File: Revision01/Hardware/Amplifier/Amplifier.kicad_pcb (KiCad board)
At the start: 2 copper layers, 23 x 13.5 mm, 13 parts, among them U1 INA333AIDGKR, U2 TLV9061SQDBVRQ1

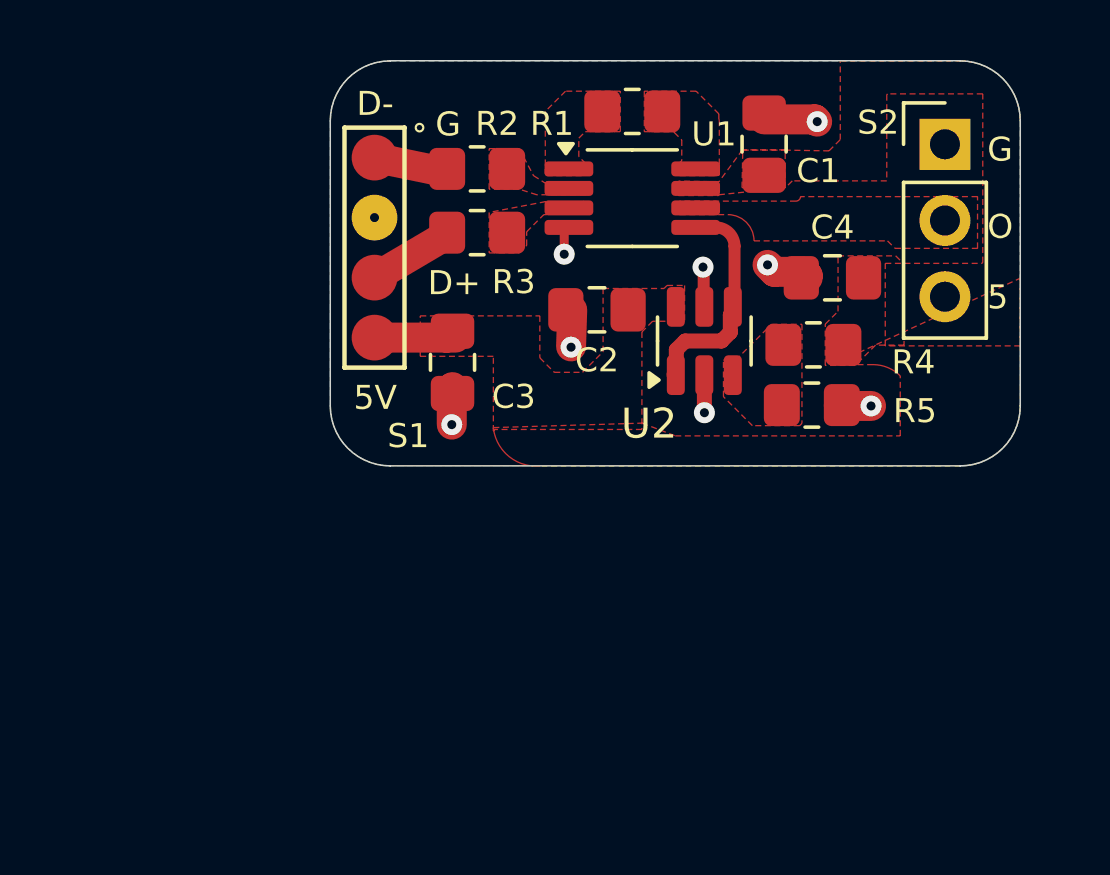
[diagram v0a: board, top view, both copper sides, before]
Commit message: . Amplifier layout WIP draft with 500 ohm resistor . Hub layout final draft, added 100 ohm series resistor to AIN
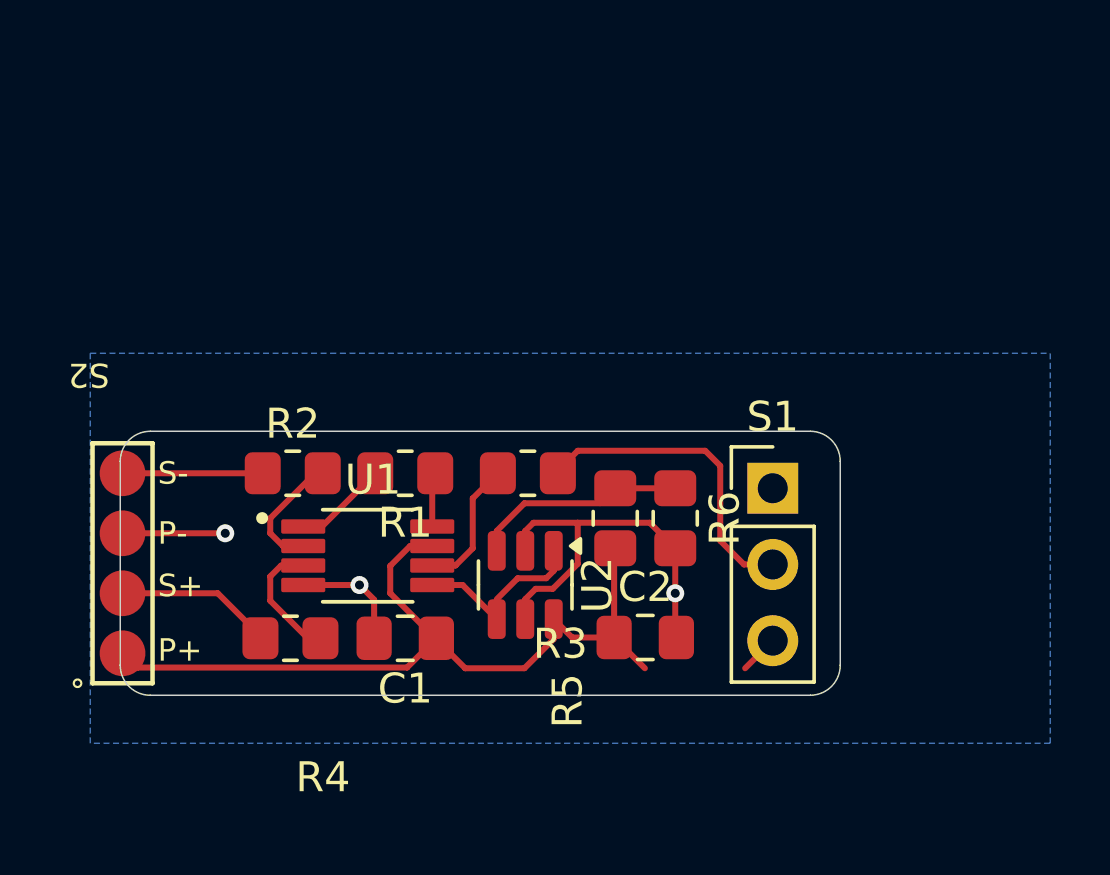
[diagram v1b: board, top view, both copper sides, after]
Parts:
- removed C3, C4: 0.1uF, Capacitor_SMD:C_0805_2012Metric_Pad1.18x1.45mm_HandSolder
- added R6: 100K +-0.1%, Resistor_SMD:R_0805_2012Metric_Pad1.20x1.40mm_HandSolder, F.Cu at (148.5, 113.5)
- R3: value 1K +-0.1% -> 500 ± 5%
- R4: value 200K +-0.1% -> 1K +-0.1%
- R5: value 100K +-0.1% -> 200K +-0.1%
- S1: value CONN_01X04_StrainGauge -> CONN_01X03_2.54MM; footprint StrainAmplifierV1:CONN_01X04 -> Connector_PinHeader_2.54mm:PinHeader_1x03_P2.54mm_Vertical
- S2: value CONN_01X03_2.54MM -> CONN_01X04_StrainGauge; footprint Connector_PinHeader_2.54mm:PinHeader_1x03_P2.54mm_Vertical -> Amplifier:CONN_01X04
- U1: footprint Package_SO:VSSOP-8_3x3mm_P0.65mm -> Amplifier:INA333AIDGKR_SOP65P490X110-8N
- moved S2 32.2 mm to (130.1, 118.0), turned to 180 degrees
- moved C1 20.4 mm to (139.5, 117.5), turned to 180 degrees
- moved R4 20.0 mm to (135.7, 117.5), turned to 180 degrees
- moved S1 17.3 mm to (151.8, 112.5)
- moved U1 14.8 mm to (138.2, 114.8)
- moved R1 14.2 mm to (139.5, 112.0)
- moved R2 11.9 mm to (135.8, 112.0), turned to 0 degrees
- moved C2 11.0 mm to (147.5, 117.5), turned to 0 degrees
- moved U2 10.1 mm to (143.5, 115.7), turned to -90 degrees
- moved R3 8.20 mm to (143.6, 112.0)
- moved R5 7.56 mm to (146.5, 113.5), turned to 90 degrees
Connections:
- R2 pad 1: Net-(U1-VIN-) -> /strainAIN_D-
- R2 pad 2: /strainAIN_D- -> Net-(U1-VIN-)
- R3 pad 1: Net-(U1-VIN+) -> Net-(S1-Pin_2)
- R3 pad 2: /strainAIN_D+ -> Net-(U1-VOUT)
- R4 pad 1: Net-(U2-IN+) -> Net-(U1-VIN+)
- R4 pad 2: +5V -> /strainAIN_D+
- R5 pad 1: GND -> +5V
- S1 pad 1: /strainAIN_D- -> GND
- S1 pad 2: GND -> Net-(S1-Pin_2)
- S1 pad 3: /strainAIN_D+ -> +5V
- S2 pad 1: GND -> +5V
- S2 pad 2: Net-(U1-VOUT) -> /strainAIN_D+
- S2 pad 3: +5V -> GND
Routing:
- net +5V: track 2.95 -> 29.7 mm
- net Net-(S1-Pin_2): track 0.00 -> 11.1 mm
- net GND: track 10.2 -> 20.3 mm, vias 8 -> 3
- net Net-(U2-IN+): track 0.00 -> 7.42 mm
- net Net-(U1-VOUT): track 0.00 -> 4.50 mm
- net Net-(U1-VIN+): track 0.00 -> 4.25 mm
- net Net-(U1-VIN-): track 0.00 -> 4.15 mm
- net Net-(R1-Pad2): track 0.00 -> 3.14 mm
- net /strainAIN_D+: track 2.90 -> 4.94 mm
- net /strainAIN_D-: track 2.48 -> 4.35 mm
- net Net-(R1-Pad1): track 0.00 -> 1.82 mm
- net Net-(U1-REF): track 7.14 -> 6.24 mm
- removed copper zone on F.Cu, net +5V
- removed copper zone on F.Cu, net Net-(R1-Pad1)
- removed copper zone on F.Cu, net Net-(R1-Pad2)
- removed copper zone on F.Cu, net Net-(U1-VIN+)
- removed copper zone on F.Cu, net Net-(U1-VIN-)
- removed copper zone on F.Cu, net Net-(U1-VOUT)
- removed copper zone on F.Cu, net Net-(U2-IN+)
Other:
- board size 23 x 13.5 mm -> 24 x 8.8 mm
- board text added: "P+"
- board text added: "P-"
- board text added: "S+"
- board text added: "S-"
- board text removed: "5"
- board text removed: "5V"
- board text removed: "D+"
- board text removed: "D-"
- board text removed: "G"
- board text removed: "O"

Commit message: . Merged Amplifier & Hub libraries into "Lib" . Added Amplifier 6 pin IDC footprint . Finalized Amplifier layout & silkscreen
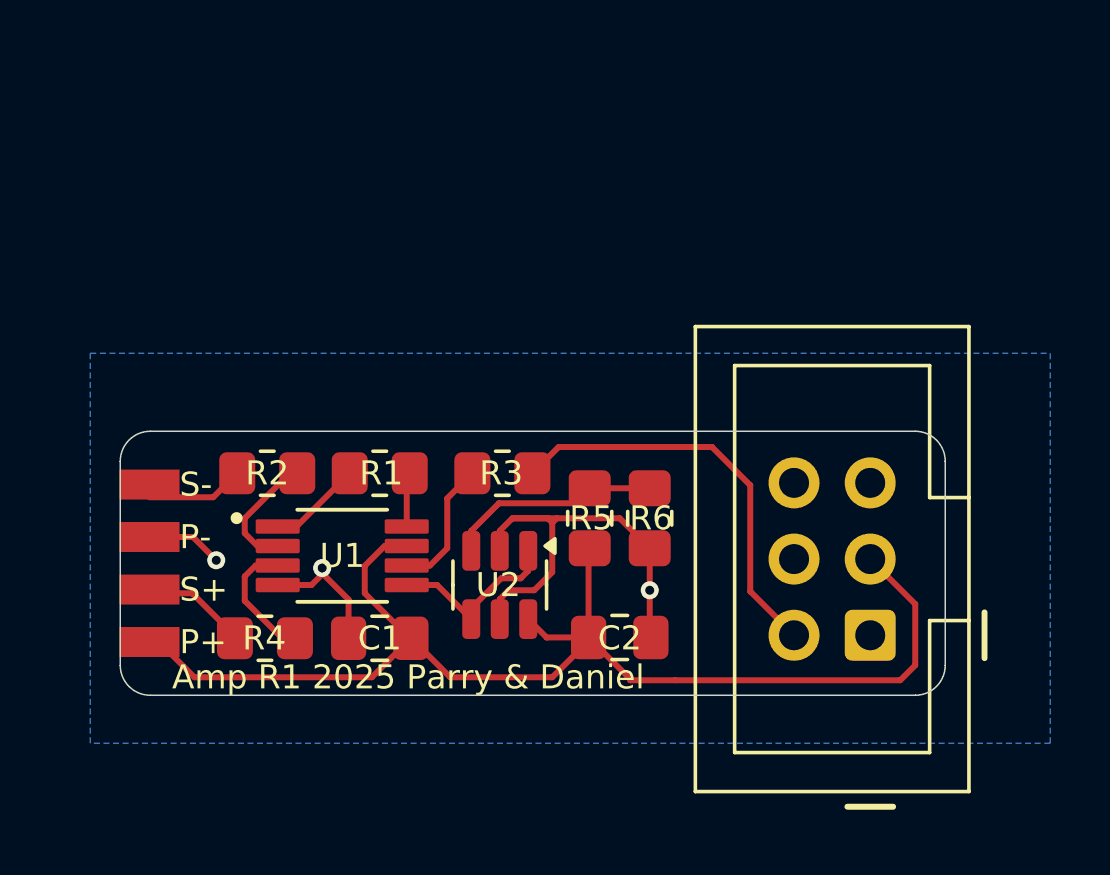
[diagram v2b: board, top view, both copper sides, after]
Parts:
- added G***: LOGO, Lib:BCIT-Racing-Logo_20mm_8mm8, B.Cu at (141.4, 115.8)
- S1: footprint Connector_PinHeader_2.54mm:PinHeader_1x03_P2.54mm_Vertical -> Lib:AdamTech_BHR-06-VUA
- S2: footprint Amplifier:CONN_01X04 -> Lib:CONN_01X04
- U1: footprint Amplifier:INA333AIDGKR_SOP65P490X110-8N -> Lib:INA333AIDGKR_SOP65P490X110-8N
- moved S1 5.88 mm to (155.0, 117.4), turned to 180 degrees
- moved C1 0.85 mm to (138.7, 117.5)
- moved C2 0.85 mm to (146.7, 117.5)
- moved R1 0.85 mm to (138.7, 112.0)
- moved R2 0.85 mm to (134.9, 112.0)
- moved R3 0.85 mm to (142.7, 112.0)
- moved R4 0.85 mm to (134.8, 117.5)
- moved R5 0.85 mm to (145.7, 113.5)
- moved R6 0.85 mm to (147.7, 113.5)
- moved U1 0.85 mm to (137.4, 114.8)
- moved U2 0.85 mm to (142.7, 115.7)
- moved S2 0.39 mm to (130.0, 117.6)
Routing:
- net +5V: track 29.7 -> 42.9 mm
- net Net-(S1-Pin_2): track 11.1 -> 14.4 mm
- net GND: track 20.3 -> 22.6 mm
- net /strainAIN_D-: track 4.35 -> 3.26 mm
- net /strainAIN_D+: track 4.94 -> 4.09 mm
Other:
- board size 24 x 8.8 mm -> 27.5 x 8.8 mm
- board text added: "Amp R1 2025 Parry & Daniel"
- board text added: "C1"
- board text added: "C2"
- board text added: "R1"
- board text added: "R2"
- board text added: "R3"
- board text added: "R4"
- board text added: "R5"
- board text added: "R6"
- board text removed: "P+"
- board text removed: "P-"
- board text removed: "S+"
- board text removed: "S-"

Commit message: . Exported BOM (.csv), gerbers & dill files, 3D Model (.step) file to Product/2025-08-16 for both Amplifier & Hub boards.
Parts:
- R5: value 200K +-0.1% -> 20K +-0.1%
- R6: value 100K +-0.1% -> 10K +-0.1%

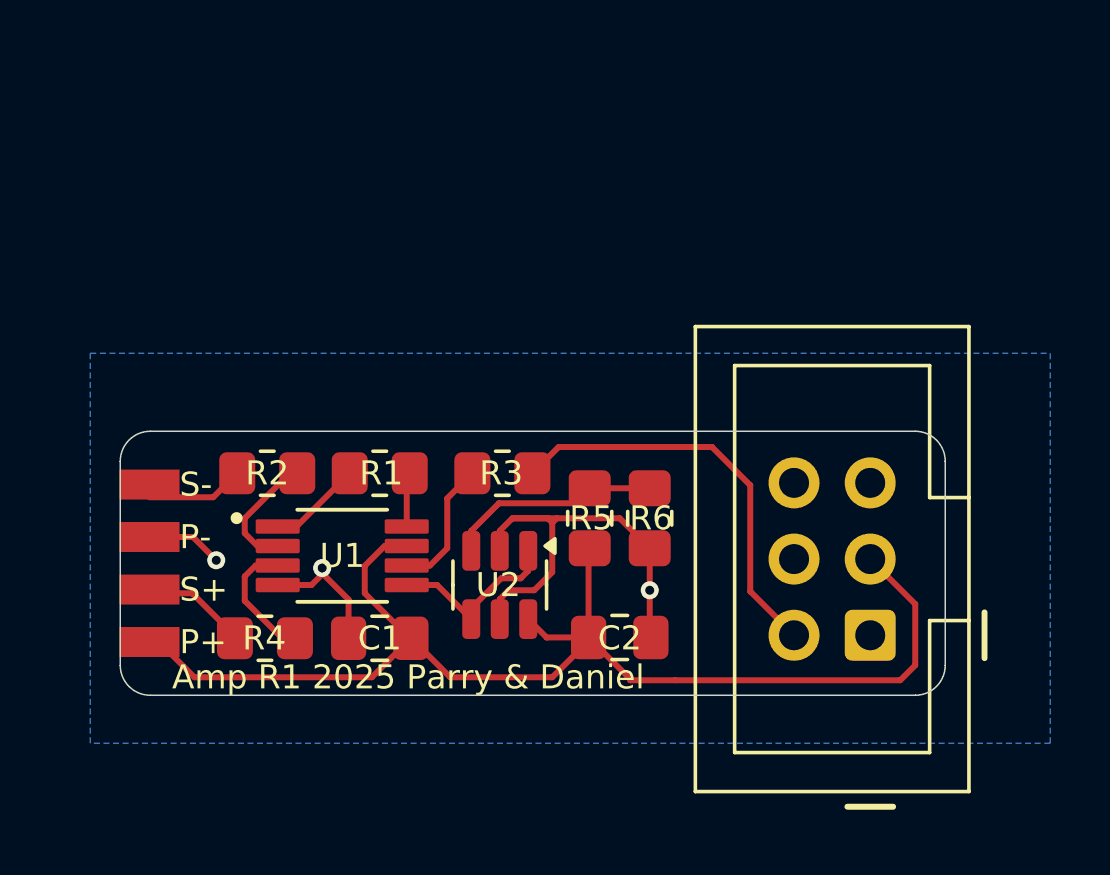
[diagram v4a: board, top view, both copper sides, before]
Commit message: . Made sure amplifier passive silk screen doesn't overlap pads . Added 6xAA battery holder to hub BOM . Exported gerbers, drl files .zip (PCBWay approved)
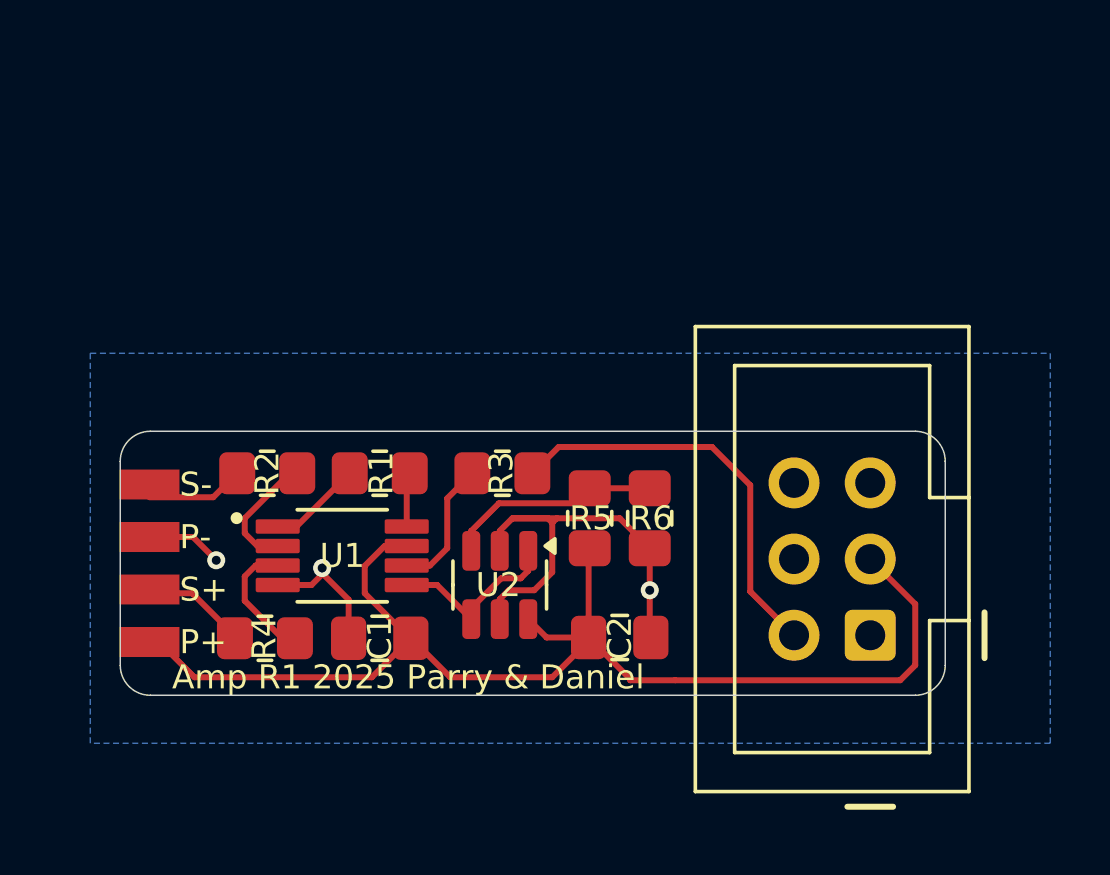
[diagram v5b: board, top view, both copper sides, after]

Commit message: . Hub & Amp: Changed wiring standard to GND SIG GND GND PWR GND . Hub: Added GND plane to 3.3V . Hub: Moved 1M pulldown resistor . Hub & Amp: Adjusted thermal relief tolerances . Hub: Changed buck convertor layout so capacitors are inline with feedback pin . Hub: Added stitching vias . Hub & Amp: Changed font sizes, changed silkscreen to be oriented one way
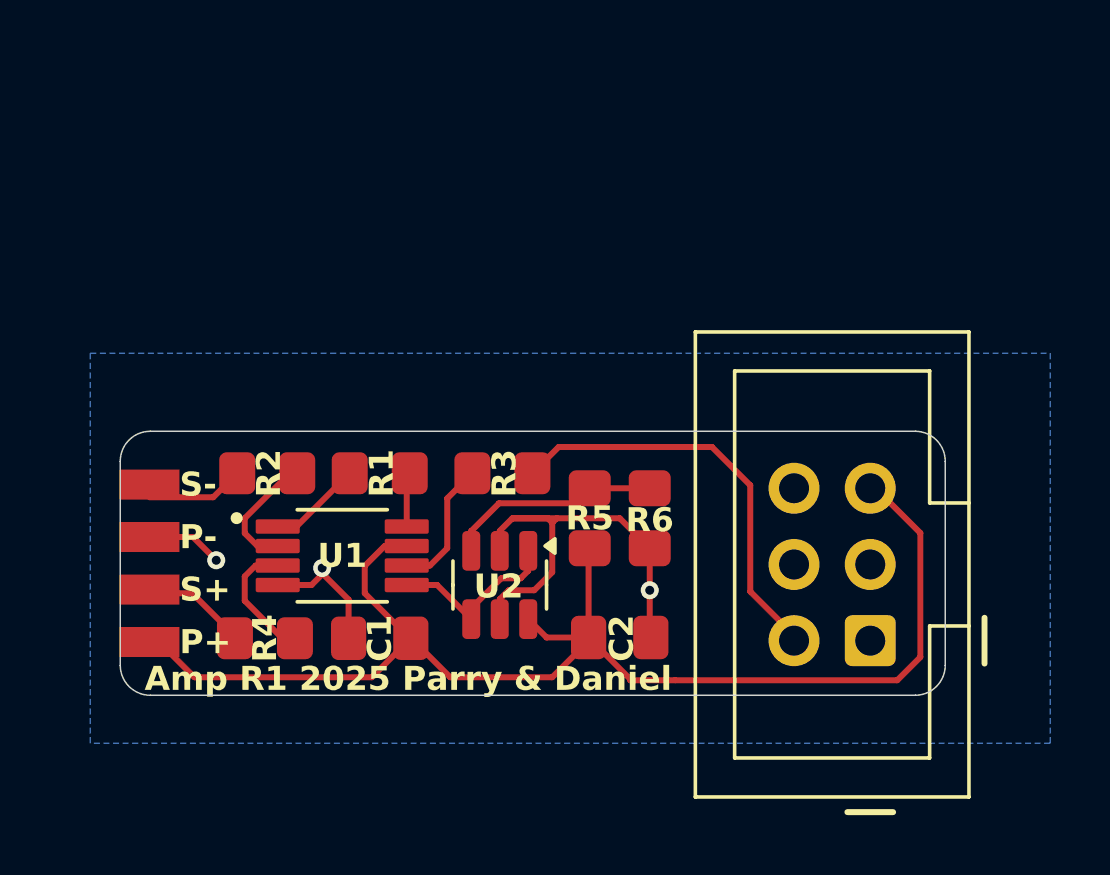
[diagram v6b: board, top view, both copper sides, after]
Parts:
- moved S1 0.18 mm to (155.0, 117.6)
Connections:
- S1 pad 3: +5V -> GND
- S1 pad 4: unconnected-(S1-Pin_4-Pad4) -> GND
- S1 pad 5: unconnected-(S1-Pin_5-Pad5) -> +5V
- S1 pad 6: unconnected-(S1-Pin_6-Pad6) -> GND
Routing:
- net +5V: track 42.9 -> 45.5 mm
